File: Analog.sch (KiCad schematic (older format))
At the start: 14 parts, among them J6 Conn_01x02, J7 Conn_02x04_Top_Bottom, J8 Conn_02x03_Top_Bottom, U2 REF5040, U3 OPA333AID, U4 50k 0.1%, U5 OPA333AID

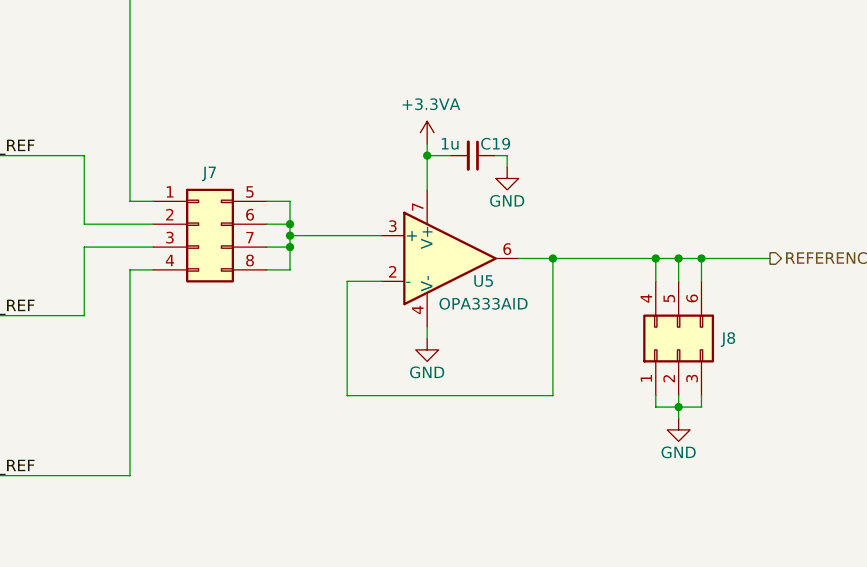
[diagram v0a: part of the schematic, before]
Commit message: MCU prepped for fanout
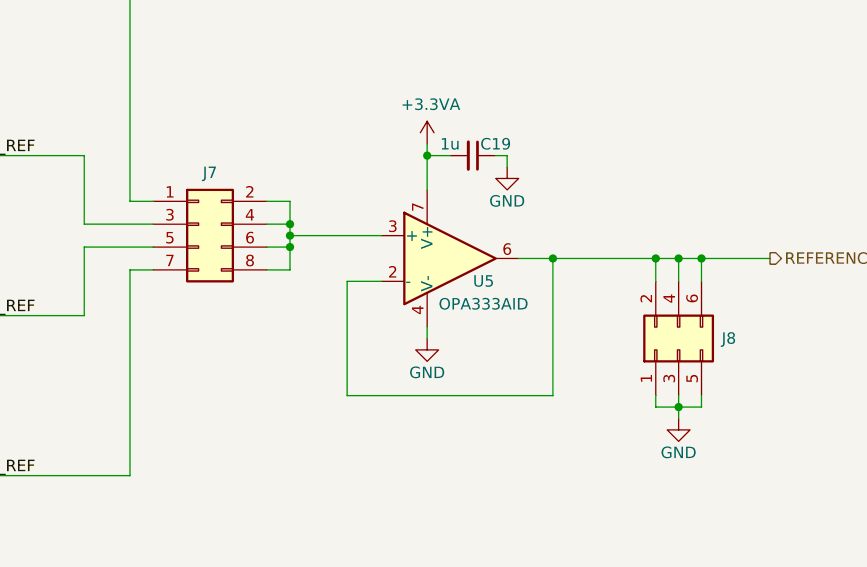
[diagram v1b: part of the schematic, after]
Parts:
- removed J7: Conn_02x04_Top_Bottom, Connector_PinHeader_2.54mm:PinHeader_2x04_P2.54mm_Vertical, symbol Connector_Generic:Conn_02x04_Top_Bottom
- removed J8: Conn_02x03_Top_Bottom, Connector_PinHeader_2.54mm:PinHeader_2x03_P2.54mm_Vertical, symbol Connector_Generic:Conn_02x03_Top_Bottom
- added J7: Conn_02x04_Odd_Even, Connector_PinHeader_2.54mm:PinHeader_2x04_P2.54mm_Vertical, symbol Connector_Generic:Conn_02x04_Odd_Even
- added J8: Conn_02x03_Odd_Even, Connector_PinHeader_2.54mm:PinHeader_2x03_P2.54mm_Vertical, symbol Connector_Generic:Conn_02x03_Odd_Even
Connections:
- net 1_4_REF: now also J7.7 (Pin_7)
- net 2_4_REF: now also J7.5 (Pin_5)
- net 3_4_REF: now also J7.3 (Pin_3)
- net GND: now also J8.1 (Pin_1), J8.3 (Pin_3), J8.5 (Pin_5)
- net REF: now also J7.1 (Pin_1)
- net REFERENCE_VOLTAGE: now also J8.2 (Pin_2), J8.4 (Pin_4), J8.6 (Pin_6)
- net at U5.3 (+): now also J7.2 (Pin_2), J7.4 (Pin_4), J7.6 (Pin_6), J7.8 (Pin_8)
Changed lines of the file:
@@
 	1    0    0    -1
-$EndComp
-$Comp
-L Connector_Generic:Conn_02x03_Top_Bottom J8
-U 1 1 600EFC9C
-P 9350 4100
-F 0 "J8" V 9400 3912 50  0000 R CNN
-F 1 "Conn_02x03_Top_Bottom" V 9355 3912 50  0001 R CNN
-F 2 "Connector_PinHeader_2.54mm:PinHeader_2x03_P2.54mm_Vertical" H 9350 4100 50  0001 C CNN
-F 3 "~" H 9350 4100 50  0001 C CNN
-	1    9350 4100
-	0    -1   -1   0
 $EndComp
 Wire Wire Line
@@
 Text HLabel 9750 3700 2    50   Output ~ 0
 REFERENCE_VOLTAGE
-$Comp
-L Connector_Generic:Conn_02x04_Top_Bottom J7
-U 1 1 6010387A
-P 7250 3550
-F 0 "J7" H 7300 3775 50  0000 C CNN
-F 1 "Conn_02x04_Top_Bottom" H 7300 3776 50  0001 C CNN
-F 2 "Connector_PinHeader_2.54mm:PinHeader_2x04_P2.54mm_Vertical" H 7250 3550 50  0001 C CNN
-F 3 "~" H 7250 3550 50  0001 C CNN
-	1    7250 3550
-	1    0    0    -1
-$EndComp
 Wire Wire Line
 	7550 3750 7650 3750
@@
 Wire Wire Line
 	5550 3250 6750 3250
+$Comp
+L Connector_Generic:Conn_02x04_Odd_Even J?
+U 1 1 5FB39908
+P 7250 3550
+AR Path="/5FA2782B/5FB39908" Ref="J?"  Part="1"
+AR Path="/5FA2666C/5FB39908" Ref="J7"  Part="1"
+F 0 "J7" H 7300 3775 50  0000 C CNN
+F 1 "Conn_02x04_Odd_Even" V 7345 3730 50  0001 L CNN
+F 2 "Connector_PinHeader_2.54mm:PinHeader_2x04_P2.54mm_Vertical" H 7250 3550 50  0001 C CNN
+F 3 "~" H 7250 3550 50  0001 C CNN
+	1    7250 3550
+	1    0    0    -1
+$EndComp
+$Comp
+L Connector_Generic:Conn_02x03_Odd_Even J8
+U 1 1 5FB4823B
+P 9350 4100
+F 0 "J8" V 9400 3912 50  0000 R CNN
+F 1 "Conn_02x03_Odd_Even" V 9355 3912 50  0001 R CNN
+F 2 "Connector_PinHeader_2.54mm:PinHeader_2x03_P2.54mm_Vertical" H 9350 4100 50  0001 C CNN
+F 3 "~" H 9350 4100 50  0001 C CNN
+	1    9350 4100
+	0    -1   -1   0
+$EndComp
 $EndSCHEMATC
